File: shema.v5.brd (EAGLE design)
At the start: 41.6 x 78.7 mm, 18 parts, among them Q1 2.5A/30V

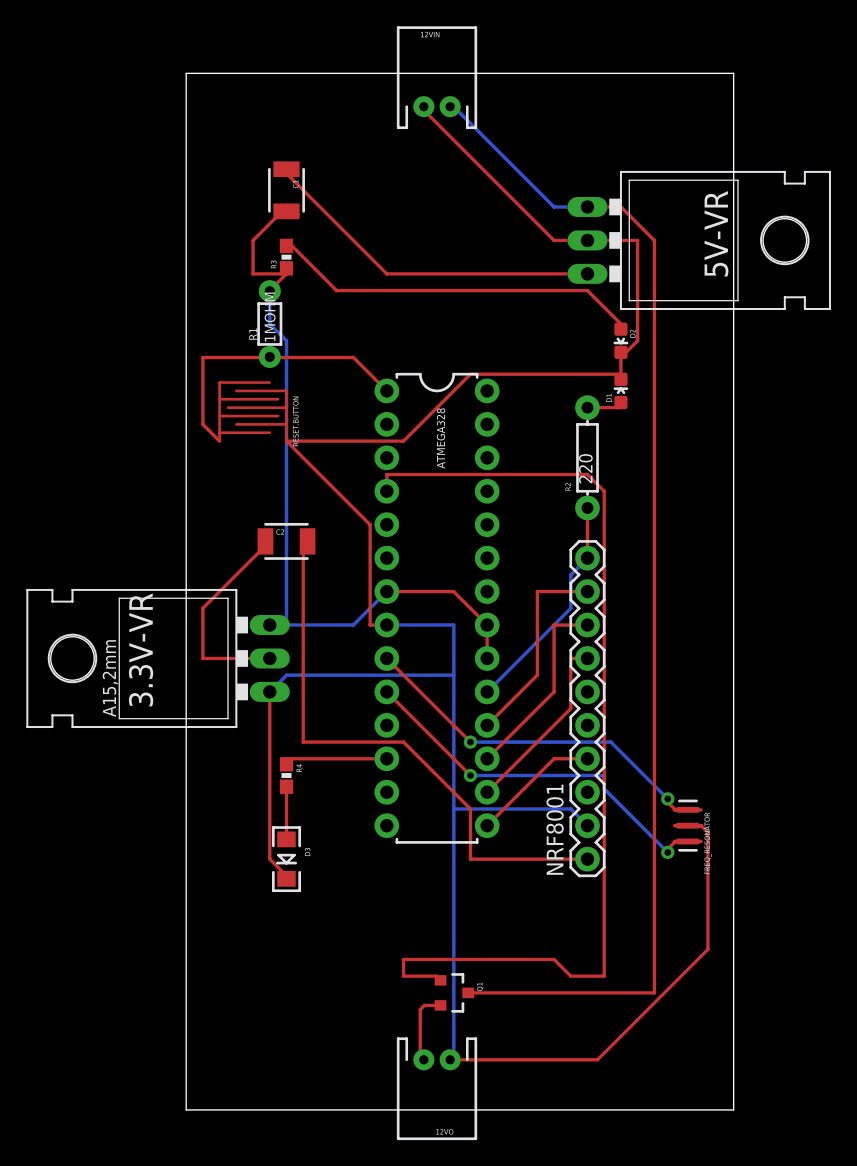
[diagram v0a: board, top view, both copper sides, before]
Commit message: Replace MOSFET
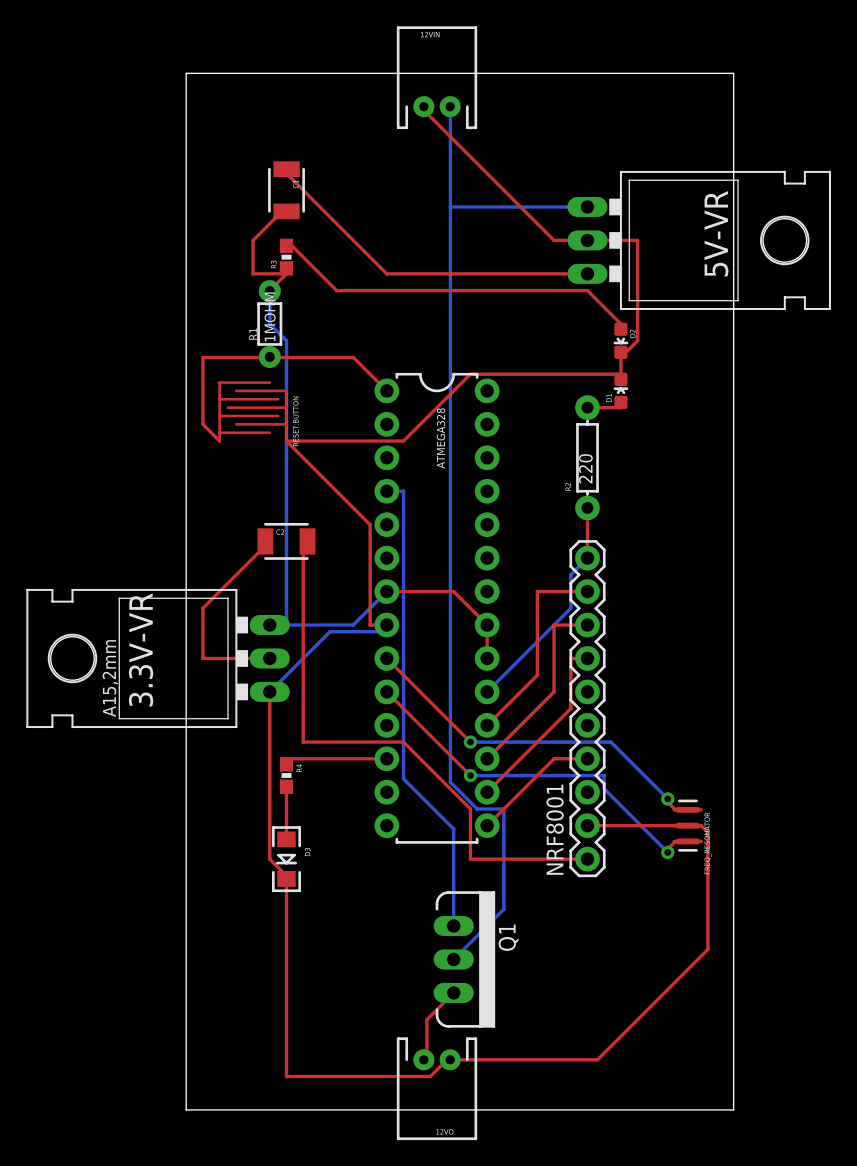
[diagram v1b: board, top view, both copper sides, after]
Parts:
- Q1: value 2.5A/30V -> MOSFET-PCHANNELNDP6020P_20V_24A_LOW_VGS_TH; device SparkFun-DiscreteSemi:SOT23-3 -> SparkFun-DiscreteSemi:TO220V
- moved Q1 2.54 mm to (54.6, 11.4)
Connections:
- net 12VIN: now also Q1.2; no longer Q1.3
- net N$4: now also Q1.3; no longer Q1.2
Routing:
- net ARDUINO.D3: track 75.1 -> 35.9 mm
- net GND: track 189.8 -> 171.8 mm
- net 12VIN: track 91.0 -> 79.7 mm
- net N$4: track 5.59 -> 6.16 mm
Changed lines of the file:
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@@
 <attribute name="PROD_ID" value="CONN-11563" x="64.77" y="19.05" size="1.778" layer="27" rot="R90" display="off"/>
 </element>
-<element name="Q1" library="SparkFun-DiscreteSemi" package="SOT23-3" value="2.5A/30V" x="54.61" y="8.89" rot="R270">
-<attribute name="PROD_ID" value="TRANS-11308" x="54.61" y="8.89" size="1.778" layer="27" rot="R270" display="off"/>
+<element name="Q1" library="SparkFun-DiscreteSemi" package="TO220V" value="MOSFET-PCHANNELNDP6020P_20V_24A_LOW_VGS_TH" x="54.61" y="11.43" rot="R270">
+<attribute name="PROD_ID" value="TRANS-13060" x="54.61" y="11.43" size="1.778" layer="27" rot="R270" display="off"/>
 </element>
 <element name="R1" library="SparkFun-Resistors" package="1/6W-RES" value="1MOHM" x="40.64" y="59.69" rot="R90"/>
@@
 <wire x1="41.91" y1="50.8" x2="50.8" y2="50.8" width="0.254" layer="1"/>
 <wire x1="67.31" y1="55.88" x2="67.31" y2="55.487" width="0.254" layer="1"/>
-<wire x1="54.61" y1="36.83" x2="54.61" y2="33.02" width="0.254" layer="16"/>
-<wire x1="54.61" y1="33.02" x2="54.61" y2="22.86" width="0.254" layer="16"/>
-<wire x1="54.61" y1="22.86" x2="54.61" y2="3.81" width="0.254" layer="16"/>
-<wire x1="49.53" y1="36.83" x2="54.61" y2="36.83" width="0.254" layer="16"/>
-<wire x1="54.61" y1="3.81" x2="54.34" y2="3.81" width="0.254" layer="16"/>
-<wire x1="63.5" y1="22.86" x2="64.77" y2="21.59" width="0.254" layer="16"/>
-<wire x1="54.61" y1="22.86" x2="63.5" y2="22.86" width="0.254" layer="16"/>
-<wire x1="41.91" y1="33.02" x2="40.64" y2="31.75" width="0.254" layer="16"/>
-<wire x1="54.61" y1="33.02" x2="41.91" y2="33.02" width="0.254" layer="16"/>
 <wire x1="73.914" y1="21.082" x2="73.406" y2="21.59" width="0.254" layer="1"/>
 <wire x1="73.914" y1="12.192" x2="73.914" y2="21.082" width="0.254" layer="1"/>
@@
 <wire x1="54.34" y1="3.81" x2="65.532" y2="3.81" width="0.254" layer="1"/>
 <wire x1="73.406" y1="21.59" x2="72.39" y2="21.59" width="0.254" layer="1"/>
+<wire x1="71.374" y1="21.59" x2="64.77" y2="21.59" width="0.254" layer="1"/>
+<wire x1="52.832" y1="2.54" x2="54.102" y2="3.81" width="0.254" layer="1"/>
+<wire x1="41.91" y1="2.54" x2="52.832" y2="2.54" width="0.254" layer="1"/>
+<wire x1="41.91" y1="17.55" x2="41.91" y2="2.54" width="0.254" layer="1"/>
+<wire x1="54.102" y1="3.81" x2="54.34" y2="3.81" width="0.254" layer="1"/>
+<wire x1="45.212" y1="36.322" x2="40.64" y2="31.75" width="0.254" layer="16"/>
+<wire x1="49.022" y1="36.322" x2="45.212" y2="36.322" width="0.254" layer="16"/>
+<wire x1="49.53" y1="36.83" x2="49.022" y2="36.322" width="0.254" layer="16"/>
 </signal>
 <signal name="3.3VIN">
@@
 </signal>
 <signal name="12VIN">
-<contactref element="Q1" pad="3"/>
+<contactref element="Q1" pad="2"/>
 <contactref element="5V-VR" pad="IN"/>
 <contactref element="12VIN" pad="2"/>
-<wire x1="69.85" y1="8.89" x2="55.71" y2="8.89" width="0.254" layer="1"/>
-<wire x1="69.85" y1="66.04" x2="69.85" y2="8.89" width="0.254" layer="1"/>
-<wire x1="67.31" y1="68.58" x2="69.85" y2="66.04" width="0.254" layer="1"/>
-<wire x1="64.77" y1="68.58" x2="67.31" y2="68.58" width="0.254" layer="1"/>
-<wire x1="62.23" y1="68.58" x2="54.61" y2="76.2" width="0.254" layer="16"/>
-<wire x1="64.77" y1="68.58" x2="62.23" y2="68.58" width="0.254" layer="16"/>
-<wire x1="54.61" y1="76.2" x2="54.34" y2="76.2" width="0.254" layer="16"/>
+<wire x1="58.42" y1="15.24" x2="54.61" y2="11.43" width="0.254" layer="16"/>
+<wire x1="58.42" y1="22.86" x2="58.42" y2="15.24" width="0.254" layer="16"/>
+<wire x1="56.388" y1="22.86" x2="58.42" y2="22.86" width="0.254" layer="16"/>
+<wire x1="54.356" y1="24.892" x2="56.388" y2="22.86" width="0.254" layer="16"/>
+<wire x1="54.356" y1="76.2" x2="54.356" y2="68.58" width="0.254" layer="16"/>
+<wire x1="54.356" y1="68.58" x2="54.356" y2="24.892" width="0.254" layer="16"/>
+<wire x1="54.356" y1="76.2" x2="54.34" y2="76.2" width="0.254" layer="16"/>
+<wire x1="54.356" y1="68.58" x2="64.77" y2="68.58" width="0.254" layer="16"/>
 </signal>
 <signal name="N$1">
@@
 <contactref element="Q1" pad="1"/>
 <contactref element="ATMEGA328" pad="4"/>
-<wire x1="66.04" y1="46.99" x2="66.04" y2="10.16" width="0.254" layer="1"/>
-<wire x1="64.77" y1="48.26" x2="66.04" y2="46.99" width="0.254" layer="1"/>
-<wire x1="49.53" y1="48.26" x2="64.77" y2="48.26" width="0.254" layer="1"/>
-<wire x1="49.53" y1="46.99" x2="49.53" y2="48.26" width="0.254" layer="1"/>
-<wire x1="66.04" y1="10.16" x2="63.5" y2="10.16" width="0.254" layer="1"/>
-<wire x1="63.5" y1="10.16" x2="62.23" y2="11.43" width="0.254" layer="1"/>
-<wire x1="62.23" y1="11.43" x2="50.8" y2="11.43" width="0.254" layer="1"/>
-<wire x1="50.8" y1="11.43" x2="50.8" y2="10.16" width="0.254" layer="1"/>
-<wire x1="50.8" y1="10.16" x2="53.29" y2="10.16" width="0.254" layer="1"/>
-<wire x1="53.29" y1="10.16" x2="53.61" y2="9.84" width="0.254" layer="1"/>
+<wire x1="54.61" y1="21.336" x2="54.61" y2="13.97" width="0.254" layer="16"/>
+<wire x1="50.8" y1="25.146" x2="54.61" y2="21.336" width="0.254" layer="16"/>
+<wire x1="50.8" y1="46.99" x2="50.8" y2="25.146" width="0.254" layer="16"/>
+<wire x1="49.53" y1="46.99" x2="50.8" y2="46.99" width="0.254" layer="16"/>
 </signal>
 <signal name="N$5">
@@
 <signal name="N$4">
 <contactref element="12VO" pad="2"/>
-<contactref element="Q1" pad="2"/>
-<wire x1="53.61" y1="7.94" x2="52.39" y2="7.94" width="0.254" layer="1"/>
-<wire x1="52.39" y1="7.94" x2="52.07" y2="7.62" width="0.254" layer="1"/>
-<wire x1="52.07" y1="7.62" x2="52.07" y2="4.08" width="0.254" layer="1"/>
-<wire x1="52.07" y1="4.08" x2="52.34" y2="3.81" width="0.254" layer="1"/>
+<contactref element="Q1" pad="3"/>
+<wire x1="52.578" y1="6.858" x2="54.61" y2="8.89" width="0.254" layer="1"/>
+<wire x1="52.578" y1="3.81" x2="52.578" y2="6.858" width="0.254" layer="1"/>
+<wire x1="52.578" y1="3.81" x2="52.34" y2="3.81" width="0.254" layer="1"/>
 </signal>
 <signal name="N$9">
